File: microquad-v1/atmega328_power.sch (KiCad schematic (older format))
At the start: 4 parts

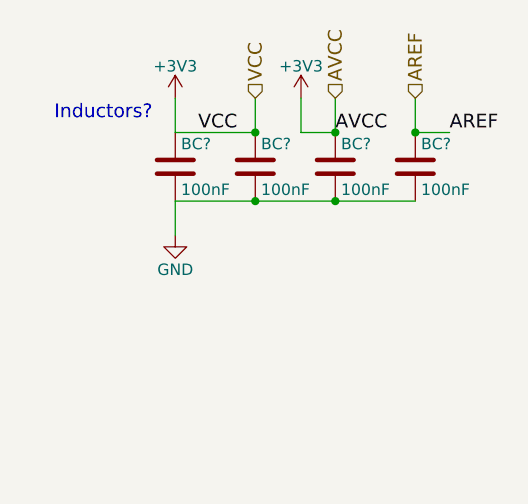
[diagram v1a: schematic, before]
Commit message: Added Hoppe's battery circuit
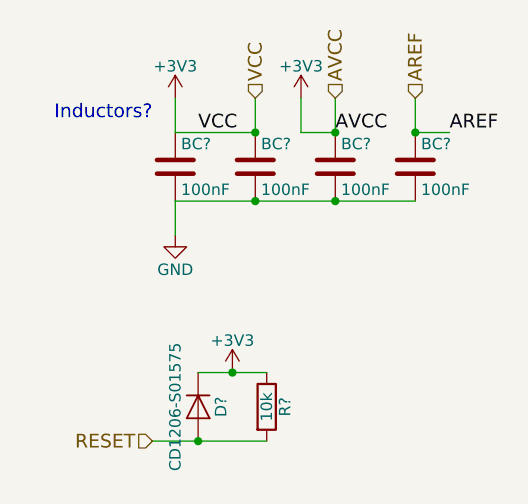
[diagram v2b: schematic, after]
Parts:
- added D?: CD1206-S01575, Capacitors_SMD:C_0402, symbol D
- added R?: 10k, Resistors_SMD:R_0603, symbol R
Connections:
- net +3V3: now also D?.1 (K), R?.1
- new net RESET: D?.2 (A), R?.2
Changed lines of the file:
@@
 LIBS:valves
 LIBS:atmega328pb
+LIBS:eclectronics
 LIBS:microquad-v1-cache
 EELAYER 25 0
@@
 $Descr A4 11693 8268
 encoding utf-8
-Sheet 4 4
+Sheet 4 5
 Title ""
 Date ""
@@
 $EndComp
 $Comp
-L GND #PWR?
+L GND #PWR015
 U 1 1 59F24A53
 P 1400 2800
-F 0 "#PWR?" H 1400 2550 50  0001 C CNN
+F 0 "#PWR015" H 1400 2550 50  0001 C CNN
 F 1 "GND" H 1400 2650 50  0000 C CNN
 F 2 "" H 1400 2800 50  0001 C CNN
@@
 $EndComp
 Wire Wire Line
-	1400 2650 2450 2650
+	1400 2650 1750 2650
+Wire Wire Line
+	1750 2650 2100 2650
+Wire Wire Line
+	2100 2650 2450 2650
 $Comp
 L C BC?
@@
 	1750 2350 1400 2350
 $Comp
-L +3V3 #PWR?
+L +3V3 #PWR016
 U 1 1 59F24D16
 P 1400 2200
-F 0 "#PWR?" H 1400 2050 50  0001 C CNN
+F 0 "#PWR016" H 1400 2050 50  0001 C CNN
 F 1 "+3V3" H 1400 2340 50  0000 C CNN
 F 2 "" H 1400 2200 50  0001 C CNN
@@
 $EndComp
 $Comp
-L +3V3 #PWR?
+L +3V3 #PWR017
 U 1 1 59F24D34
 P 1950 2200
-F 0 "#PWR?" H 1950 2050 50  0001 C CNN
+F 0 "#PWR017" H 1950 2050 50  0001 C CNN
 F 1 "+3V3" H 1950 2340 50  0000 C CNN
 F 2 "" H 1950 2200 50  0001 C CNN
@@
 Text Label 2600 2350 0    60   ~ 0
 AREF
+Text HLabel 1300 3700 0    60   Input ~ 0
+RESET
+$Comp
+L +3V3 #PWR018
+U 1 1 59F50B66
+P 1650 3400
+F 0 "#PWR018" H 1650 3250 50  0001 C CNN
+F 1 "+3V3" H 1650 3540 50  0000 C CNN
+F 2 "" H 1650 3400 50  0001 C CNN
+F 3 "" H 1650 3400 50  0001 C CNN
+	1    1650 3400
+	1    0    0    -1
+$EndComp
+$Comp
+L D D?
+U 1 1 59F50B83
+P 1500 3550
+F 0 "D?" H 1500 3650 50  0000 C CNN
+F 1 "CD1206-S01575" H 1500 3450 50  0000 C CNN
+F 2 "Capacitors_SMD:C_0402" H 1500 3550 50  0001 C CNN
+F 3 "" H 1500 3550 50  0001 C CNN
+	1    1500 3550
+	0    1    1    0
+$EndComp
+Wire Wire Line
+	1500 3400 1650 3400
+Wire Wire Line
+	1650 3400 1800 3400
+$Comp
+L R R?
+U 1 1 59F50E25
+P 1800 3550
+F 0 "R?" V 1880 3550 50  0000 C CNN
+F 1 "10k" V 1800 3550 50  0000 C CNN
+F 2 "Resistors_SMD:R_0603" V 1730 3550 50  0001 C CNN
+F 3 "" H 1800 3550 50  0001 C CNN
+	1    1800 3550
+	1    0    0    -1
+$EndComp
+Connection ~ 1650 3400
+Wire Wire Line
+	1300 3700 1500 3700
+Wire Wire Line
+	1500 3700 1800 3700
+Connection ~ 1500 3700
 $EndSCHEMATC
